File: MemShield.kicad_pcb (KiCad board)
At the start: 6 copper layers, 53 x 40 mm, 124 parts, among them J1 Micro-SD Slot, J10 Molex expansions, J11 Molex expansions, J12 Molex expansions, J13 Molex expansions, J14 Solder Jumper, J15 Solder Jumper, J16 Solder Jumper, J17 Solder Jumper, J18 Solder Jumper, J19 Solder Jumper, J2 Solder Jumper, J20 Solder Jumper, J21 Solder Jumper, J3 Solder Jumper, J4 Solder Jumper, J5 Solder Jumper, J6 Solder Jumper, J7 Solder Jumper, J8 Solder Jumper, J9 Solder Jumper, M1 Microphone, M2 Microphone, M3 Microphone, M4 Microphone, M5 Microphone, M7 Microphone, P1 Crazyflie Female Expansion, P2 Crazyflie Female Expansion, P3 6220XX21121_62201021121, P5 GRPB042VWVN-RC, SW1 Test Pad, U1 AUDIO_CLK_GEN, U2 TPS63001DRCR, U3 STM32U575RGT6, U4 DS28E05R+T, X1 24MHz

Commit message: seb commit
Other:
- rule pad_to_mask_clearance: 0.05 -> 0
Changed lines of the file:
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@@
 			(dielectric_constraints no)
 		)
-		(pad_to_mask_clearance 0.05)
+		(pad_to_mask_clearance 0)
 		(allow_soldermask_bridges_in_footprints no)
 		(tenting front back)
@@
 			(plot_on_all_layers_selection 0x00000000_00000000_00000000_00000000)
 			(disableapertmacros no)
-			(usegerberextensions no)
+			(usegerberextensions yes)
 			(usegerberattributes yes)
 			(usegerberadvancedattributes yes)
-			(creategerberjobfile yes)
+			(creategerberjobfile no)
 			(dashed_line_dash_ratio 12.000000)
 			(dashed_line_gap_ratio 3.000000)
@@
 			(plotpadnumbers no)
 			(hidednponfab no)
-			(sketchdnponfab yes)
-			(crossoutdnponfab yes)
-			(subtractmaskfromsilk no)
+			(sketchdnponfab no)
+			(crossoutdnponfab no)
+			(subtractmaskfromsilk yes)
 			(outputformat 1)
 			(mirror no)

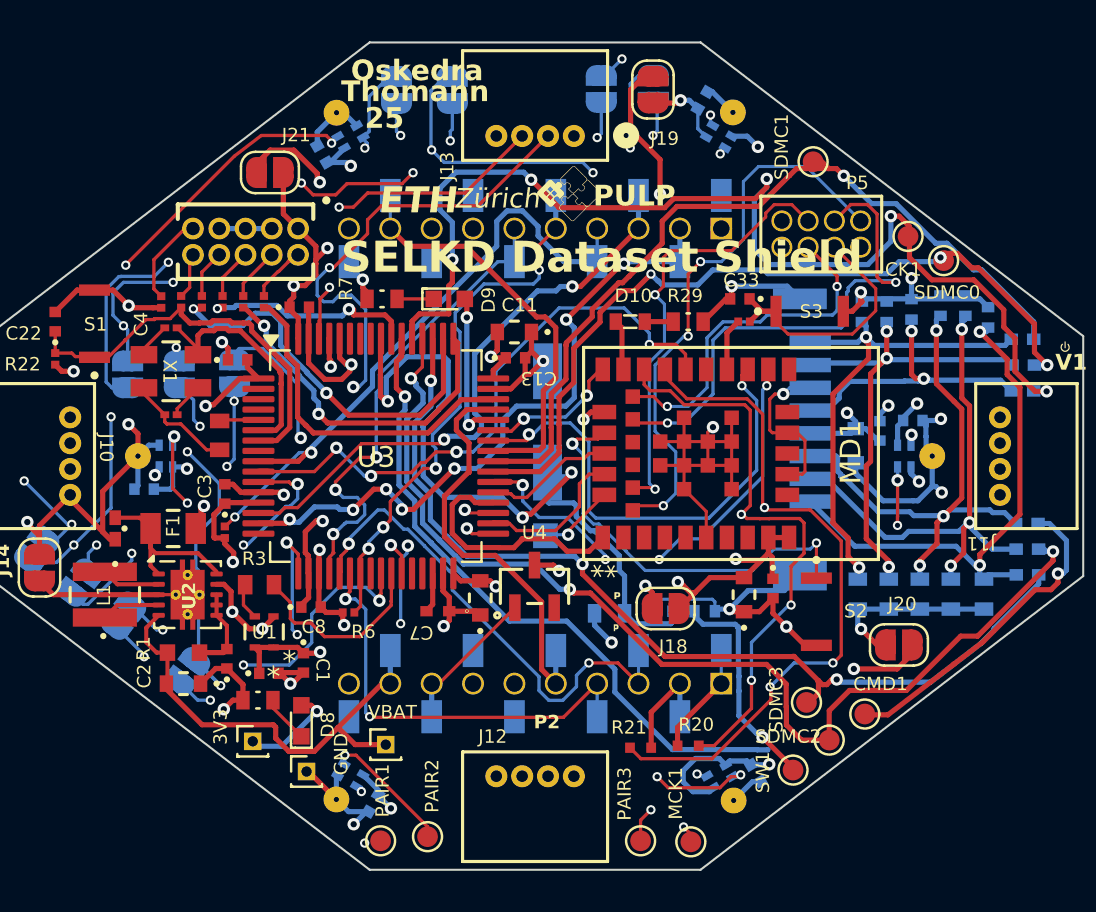
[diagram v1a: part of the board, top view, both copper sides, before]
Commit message: fixes v1
sd cmd line
sd resistors
designator placement
mirrored microphones
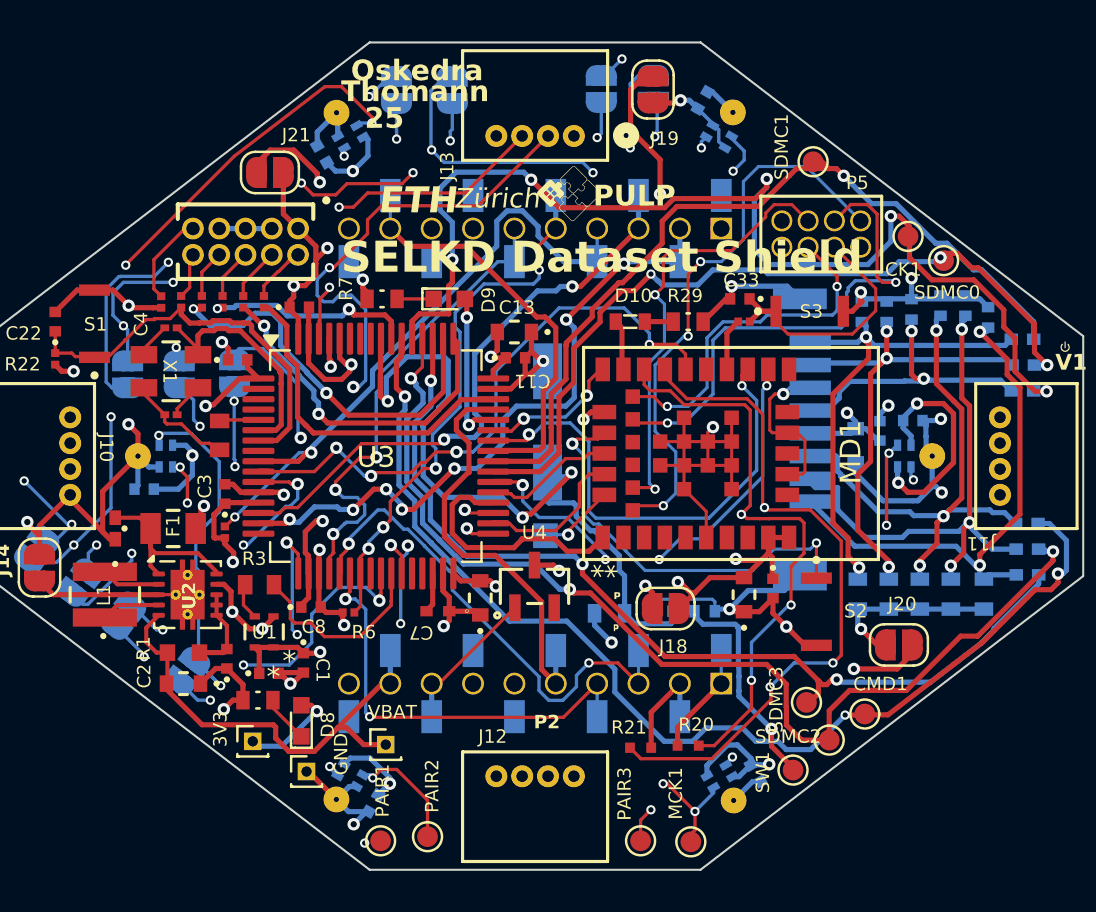
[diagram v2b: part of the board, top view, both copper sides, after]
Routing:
- net VMIC: track 23.2 -> 35.1 mm, vias 8 -> 7
- net /Core/SDMMC1.CMD: track 48.7 -> 54.7 mm, vias 2 -> 3
- net /microphones/D2_REP: track 87.2 -> 89.8 mm
- net /microphones/D1_REP: track 83.4 -> 85.1 mm, vias 4 -> 5
- net /microphones/CK_IN: track 119.0 -> 117.7 mm, vias 12 -> 10
- net /microphones/D3_REP: track 99.2 -> 98.4 mm
- net Net-(J1-CD/DAT3): track 25.4 -> 26.1 mm
